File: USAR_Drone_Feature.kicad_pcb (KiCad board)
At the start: 4 copper layers, 50 x 50 mm, 63 parts, among them CN1 B2B-XH-A, CN2 B2B-XH-A, J3 Conn_02x04_Odd_Even, J4 Conn_01x04_Socket, J5 Conn_01x04_Socket, J6 Conn_01x04_Socket, SW1 TS-1088-AR02016, SW2 TS-1088-AR02016, U1 ESP32-S3-WROOM-1(N16R8), U2 TPS62172DSG, U3 TPS62133

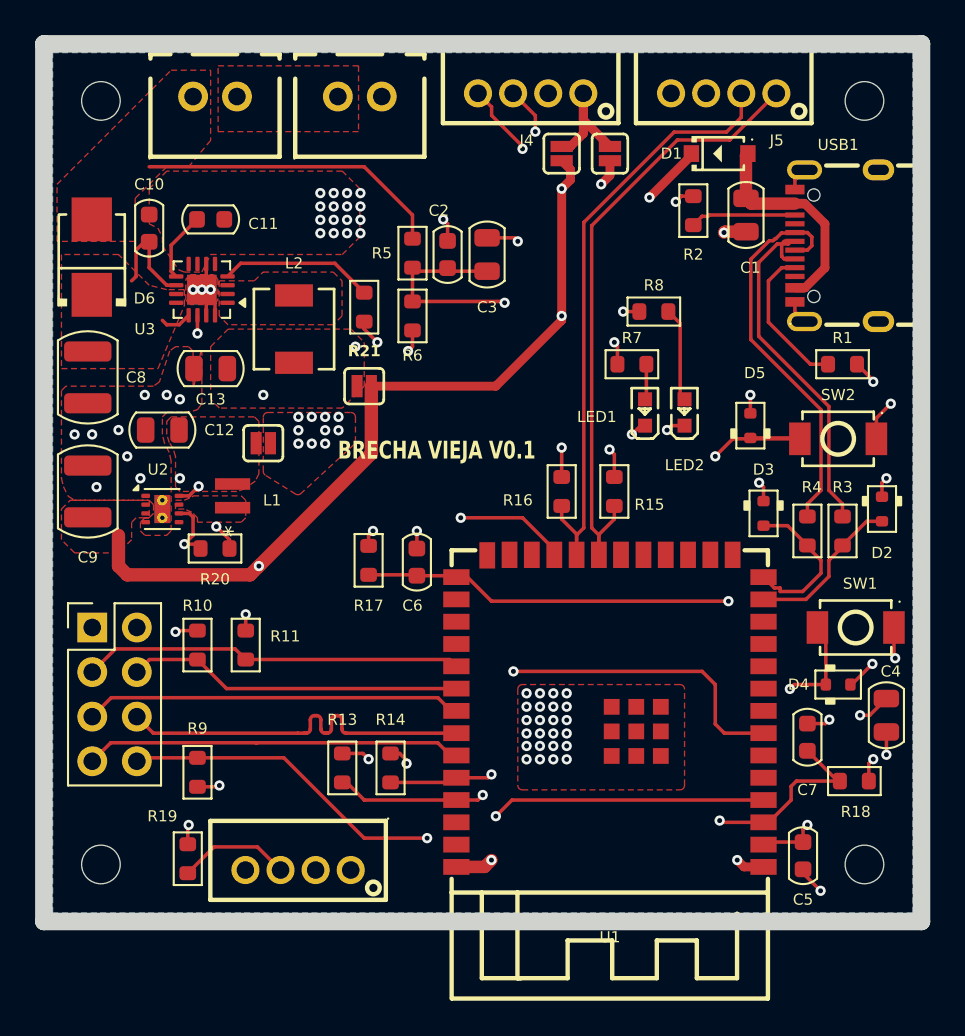
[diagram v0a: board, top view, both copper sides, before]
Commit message: cambio agujeros 2.2mm a 2.5mm
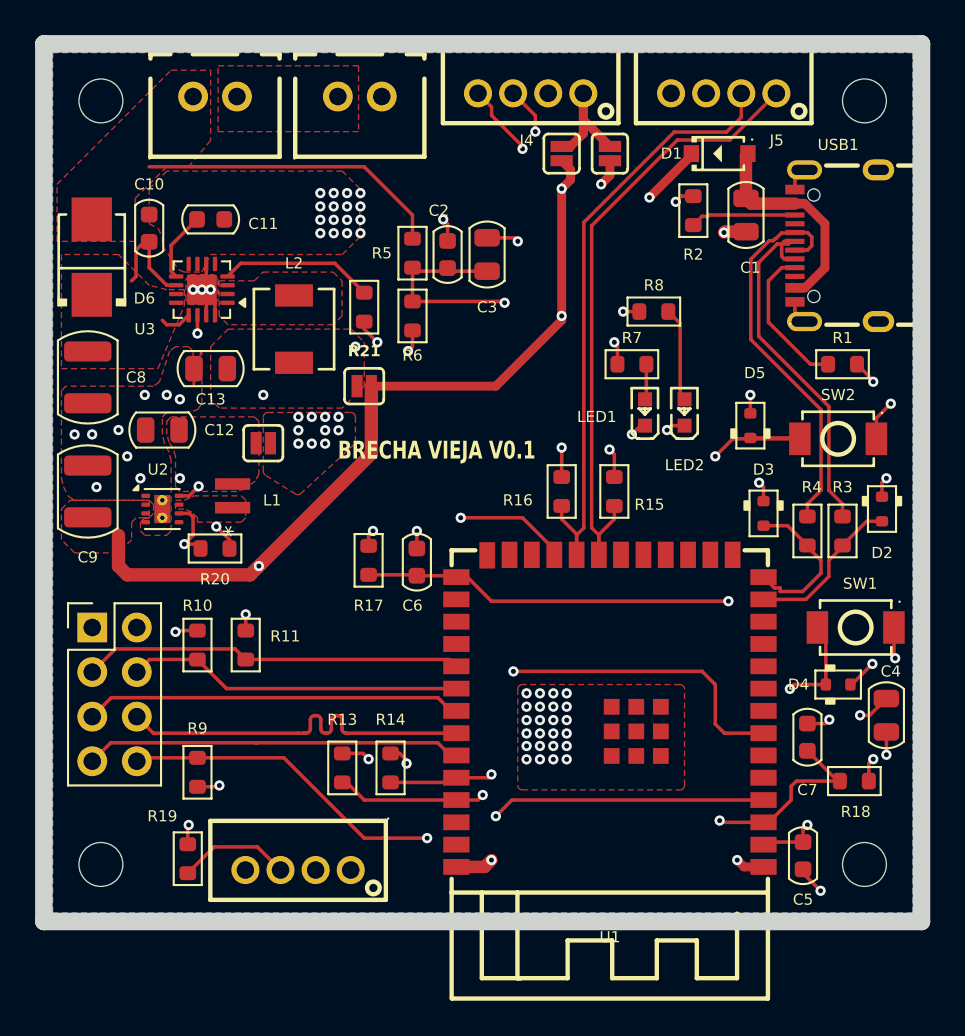
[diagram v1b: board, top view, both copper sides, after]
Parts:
- H1, H2, H3, H4: footprint MountingHole:MountingHole_2.2mm_M2_DIN965 -> MountingHole:MountingHole_2.5mm
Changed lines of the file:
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@@
 		(sheetname "/")
 		(sheetfile "USAR_Drone_Feature.kicad_sch")
+		(units
+			(unit
+				(name "A")
+				(pins "2" "11" "9" "3" "14" "13" "6" "8" "7" "5" "4" "10" "1" "12")
+			)
+		)
 		(attr smd)
 		(duplicate_pad_numbers_are_jumpers no)
@@
 		)
 	)
-	(footprint "MountingHole:MountingHole_2.2mm_M2_DIN965"
+	(footprint "MountingHole:MountingHole_2.5mm"
 		(locked yes)
 		(layer "F.Cu")
 		(at 179.55 126.85)
-		(descr "Mounting Hole 2.2mm, M2, no annular, generated by kicad-footprint-generator mountinghole.py")
-		(tags "mountinghole M2 DIN965")
+		(descr "Mounting Hole 2.5mm, no annular, generated by kicad-footprint-generator mountinghole.py")
+		(tags "mountinghole")
 		(property "Reference" "H2"
-			(at 0 -2.85 0)
+			(at 0 -3.45 0)
 			(layer "F.SilkS")
 			(hide yes)
 			(effects
 				(font
-					(size 0.635 0.635)
-					(thickness 0.14986)
+					(size 1 1)
+					(thickness 0.15)
 				)
 			)
 		)
 		(property "Value" "MountingHole"
-			(at 0 2.85 0)
+			(at 0 3.45 0)
 			(layer "F.Fab")
 			(hide yes)
 			(effects
 				(font
-					(size 0.635 0.635)
-					(thickness 0.14986)
+					(size 1 1)
+					(thickness 0.15)
 				)
 			)
@@
 		(fp_circle
 			(center 0 0)
-			(end 1.9 0)
+			(end 2.5 0)
 			(stroke
 				(width 0.15)
@@
 		(fp_circle
 			(center 0 0)
-			(end 2.15 0)
+			(end 2.75 0)
 			(stroke
 				(width 0.05)
@@
 			(effects
 				(font
-					(size 0.635 0.635)
-					(thickness 0.14986)
+					(size 1 1)
+					(thickness 0.15)
 				)
 			)
@@
 		(pad "" np_thru_hole circle
 			(at 0 0)
-			(size 2.2 2.2)
-			(drill 2.2)
+			(size 2.5 2.5)
+			(drill 2.5)
 			(layers "*.Cu" "*.Mask")
 		)
@@
 		(sheetname "/PowerRails/")
 		(sheetfile "BuckConverter.kicad_sch")
+		(units
+			(unit
+				(name "A")
+				(pins "13" "9" "8" "7" "10" "11" "12" "6" "15" "16" "17" "1" "2" "3"
+					"14" "4" "5"
+				)
+			)
+		)
 		(attr smd exclude_from_bom)
 		(duplicate_pad_numbers_are_jumpers no)
@@
 		)
 	)
-	(footprint "MountingHole:MountingHole_2.2mm_M2_DIN965"
+	(footprint "MountingHole:MountingHole_2.5mm"
 		(locked yes)
 		(layer "F.Cu")
 		(at 223.05 83.35)
-		(descr "Mounting Hole 2.2mm, M2, no annular, generated by kicad-footprint-generator mountinghole.py")
-		(tags "mountinghole M2 DIN965")
+		(descr "Mounting Hole 2.5mm, no annular, generated by kicad-footprint-generator mountinghole.py")
+		(tags "mountinghole")
 		(property "Reference" "H4"
-			(at 0 -2.85 0)
+			(at 0 -3.45 0)
 			(layer "F.SilkS")
 			(hide yes)
 			(effects
 				(font
-					(size 0.635 0.635)
-					(thickness 0.14986)
+					(size 1 1)
+					(thickness 0.15)
 				)
 			)
 		)
 		(property "Value" "MountingHole"
-			(at 0 2.85 0)
+			(at 0 3.45 0)
 			(layer "F.Fab")
 			(hide yes)
 			(effects
 				(font
-					(size 0.635 0.635)
-					(thickness 0.14986)
+					(size 1 1)
+					(thickness 0.15)
 				)
 			)
@@
 		(fp_circle
 			(center 0 0)
-			(end 1.9 0)
+			(end 2.5 0)
 			(stroke
 				(width 0.15)
@@
 		(fp_circle
 			(center 0 0)
-			(end 2.15 0)
+			(end 2.75 0)
 			(stroke
 				(width 0.05)
@@
 			(effects
 				(font
-					(size 0.635 0.635)
-					(thickness 0.14986)
+					(size 1 1)
+					(thickness 0.15)
 				)
 			)
@@
 		(pad "" np_thru_hole circle
 			(at 0 0)
-			(size 2.2 2.2)
-			(drill 2.2)
+			(size 2.5 2.5)
+			(drill 2.5)
 			(layers "*.Cu" "*.Mask")
 		)
@@
 		)
 	)
-	(footprint "MountingHole:MountingHole_2.2mm_M2_DIN965"
+	(footprint "MountingHole:MountingHole_2.5mm"
 		(locked yes)
 		(layer "F.Cu")
 		(at 223.05 126.85)
-		(descr "Mounting Hole 2.2mm, M2, no annular, generated by kicad-footprint-generator mountinghole.py")
-		(tags "mountinghole M2 DIN965")
+		(descr "Mounting Hole 2.5mm, no annular, generated by kicad-footprint-generator mountinghole.py")
+		(tags "mountinghole")
 		(property "Reference" "H3"
-			(at 0 -2.85 0)
+			(at 0 -3.45 0)
 			(layer "F.SilkS")
 			(hide yes)
 			(effects
 				(font
-					(size 0.635 0.635)
-					(thickness 0.14986)
+					(size 1 1)
+					(thickness 0.15)
 				)
 			)
 		)
 		(property "Value" "MountingHole"
-			(at 0 2.85 0)
+			(at 0 3.45 0)
 			(layer "F.Fab")
 			(hide yes)
 			(effects
 				(font
-					(size 0.635 0.635)
-					(thickness 0.14986)
+					(size 1 1)
+					(thickness 0.15)
 				)
 			)
@@
 		(fp_circle
 			(center 0 0)
-			(end 1.9 0)
+			(end 2.5 0)
 			(stroke
 				(width 0.15)
@@
 		(fp_circle
 			(center 0 0)
-			(end 2.15 0)
+			(end 2.75 0)
 			(stroke
 				(width 0.05)
@@
 			(effects
 				(font
-					(size 0.635 0.635)
-					(thickness 0.14986)
+					(size 1 1)
+					(thickness 0.15)
 				)
 			)
@@
 		(pad "" np_thru_hole circle
 			(at 0 0)
-			(size 2.2 2.2)
-			(drill 2.2)
+			(size 2.5 2.5)
+			(drill 2.5)
 			(layers "*.Cu" "*.Mask")
 		)
@@
 		(sheetname "/PowerRails/")
 		(sheetfile "BuckConverter.kicad_sch")
+		(units
+			(unit
+				(name "A")
+				(pins "2" "1")
+			)
+		)
 		(attr smd exclude_from_bom)
 		(duplicate_pad_numbers_are_jumpers no)
@@
 		)
 	)
-	(footprint "MountingHole:MountingHole_2.2mm_M2_DIN965"
+	(footprint "MountingHole:MountingHole_2.5mm"
 		(locked yes)
 		(layer "F.Cu")
 		(at 179.55 83.35)
-		(descr "Mounting Hole 2.2mm, M2, no annular, generated by kicad-footprint-generator mountinghole.py")
-		(tags "mountinghole M2 DIN965")
+		(descr "Mounting Hole 2.5mm, no annular, generated by kicad-footprint-generator mountinghole.py")
+		(tags "mountinghole")
 		(property "Reference" "H1"
-			(at 0 -2.85 0)
+			(at 0 -3.45 0)
 			(layer "F.SilkS")
 			(hide yes)
 			(effects
 				(font
-					(size 0.635 0.635)
-					(thickness 0.14986)
+					(size 1 1)
+					(thickness 0.15)
 				)
 			)
 		)
 		(property "Value" "MountingHole"
-			(at 0 2.85 0)
+			(at 0 3.45 0)
 			(layer "F.Fab")
 			(hide yes)
 			(effects
 				(font
-					(size 0.635 0.635)
-					(thickness 0.14986)
+					(size 1 1)
+					(thickness 0.15)
 				)
 			)
@@
 		(fp_circle
 			(center 0 0)
-			(end 1.9 0)
+			(end 2.5 0)
 			(stroke
 				(width 0.15)
@@
 		(fp_circle
 			(center 0 0)
-			(end 2.15 0)
+			(end 2.75 0)
 			(stroke
 				(width 0.05)
@@
 			(effects
 				(font
-					(size 0.635 0.635)
-					(thickness 0.14986)
+					(size 1 1)
+					(thickness 0.15)
 				)
 			)
@@
 		(pad "" np_thru_hole circle
 			(at 0 0)
-			(size 2.2 2.2)
-			(drill 2.2)
+			(size 2.5 2.5)
+			(drill 2.5)
 			(layers "*.Cu" "*.Mask")
 		)
@@
 			(keep_text_aligned yes)
 		)
-		(gr_text "1968.5039"
+		(gr_text "50"
 			(at 244.15 105.1 90)
 			(layer "User.2")
@@
 			(keep_text_aligned yes)
 		)
-		(gr_text "1968.5039"
+		(gr_text "50"
 			(at 201.3 145.45 0)
 			(layer "User.2")

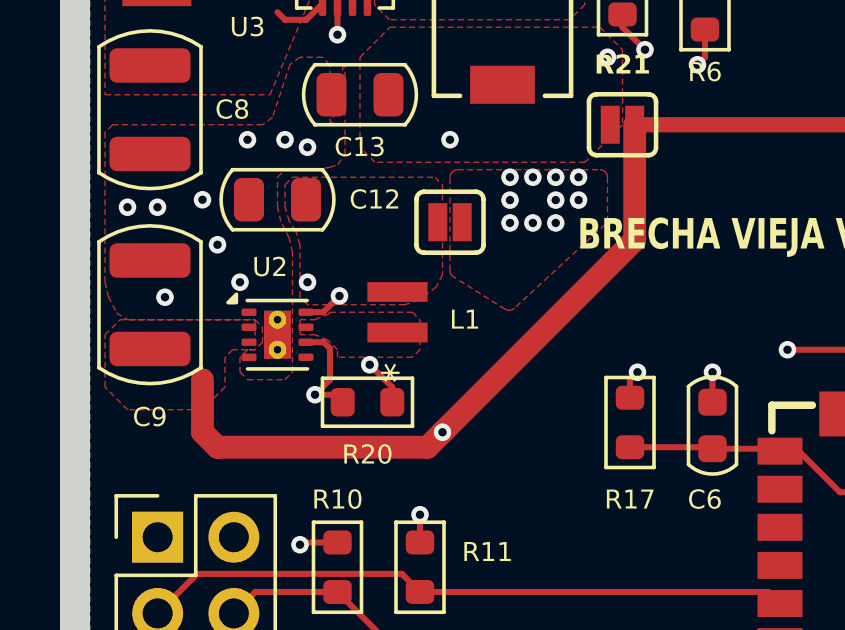
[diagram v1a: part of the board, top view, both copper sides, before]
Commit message: cambiar bobina de power suppy
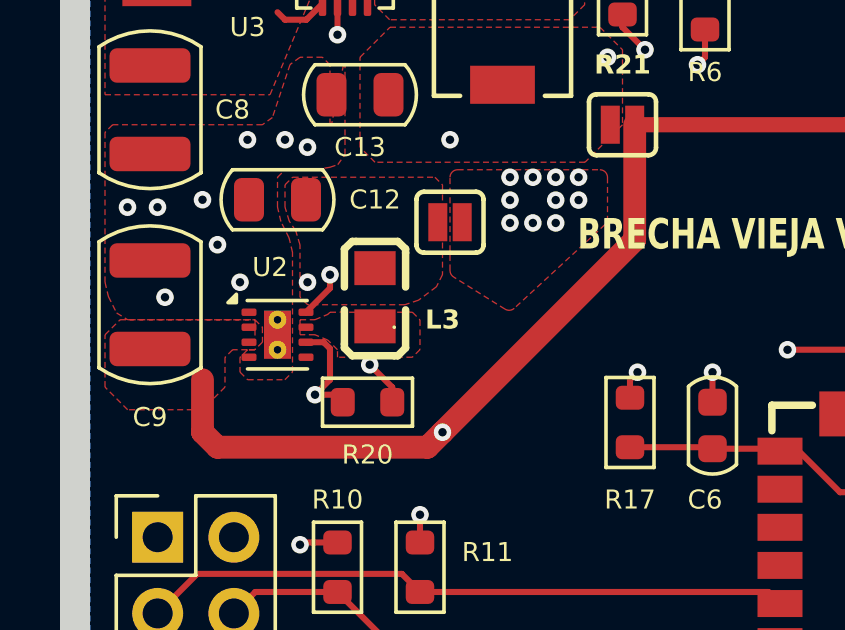
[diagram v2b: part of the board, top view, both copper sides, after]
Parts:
- removed L1: MDMK2020T2R2MM, Snapeda:IND_MDMK2020T1R0MM_TAY
- added L3: MLP2012H2R2MT0S1, EasyEDA:L0805, F.Cu at (186.3, 105.3)
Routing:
- net /PowerRails/PG2: track 6.09 -> 6.69 mm

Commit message: ajustes finales
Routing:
- net /MISO: track 21.7 -> 18.6 mm
- net /UART_P: track 51.6 -> 50.6 mm
- net /SERVO_PWM: track 42.9 -> 43.6 mm
- added copper zone on In2.Cu, net +3V3
- added copper zone on In1.Cu, net GND
- removed copper zone on In1.Cu, net +3V3
- removed copper zone on B.Cu, net GND

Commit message: stable
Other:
- board text removed: "BRECHA VIEJA V0.1"
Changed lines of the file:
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@@
 		(layer "Edge.Cuts")
-	)
-	(gr_text "BRECHA VIEJA V0.1"
-		(at 193.05 103.85 0)
-		(layer "F.SilkS")
-		(effects
-			(font
-				(size 1.016 0.762)
-				(thickness 0.1524)
-				(bold yes)
-			)
-			(justify left bottom)
-		)
 	)
 	(dimension
